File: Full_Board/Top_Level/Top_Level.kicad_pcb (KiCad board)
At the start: 2 copper layers, 187 parts, among them IC1 DRV8824QPWPRQ1, IC2 DRV8824QPWPRQ1, IC3 DRV8824QPWPRQ1, IC4 LM2576HVS-5.0_NOPB, IC5 CD74HC4051PWT, IC6 CD74HC4051PWT, IC7 DRV8210DRLR, J1 OQ0432500000G, J1-J3 Conn_01x10, J10 OQ0432500000G, J11 OQ0432500000G, J12 OQ0432500000G, J13 OQ0432500000G, J14 OQ0432500000G, J15 OQ0432500000G, J16 OQ0432500000G, J17 OQ0432500000G, J2 OQ0432500000G, J3 OQ0432500000G, J4 OQ0432500000G, J4-J2 Conn_01x10, J5 OQ0212500000G, J5-J7 Conn_01x10, J6 OQ0212500000G, J7 OQ0212500000G, J8 KLDHCX-8-0202-A, J8-J6 Conn_01x10, J9 OQ0212500000G, U1 LM2576SX-3.3-NOPB

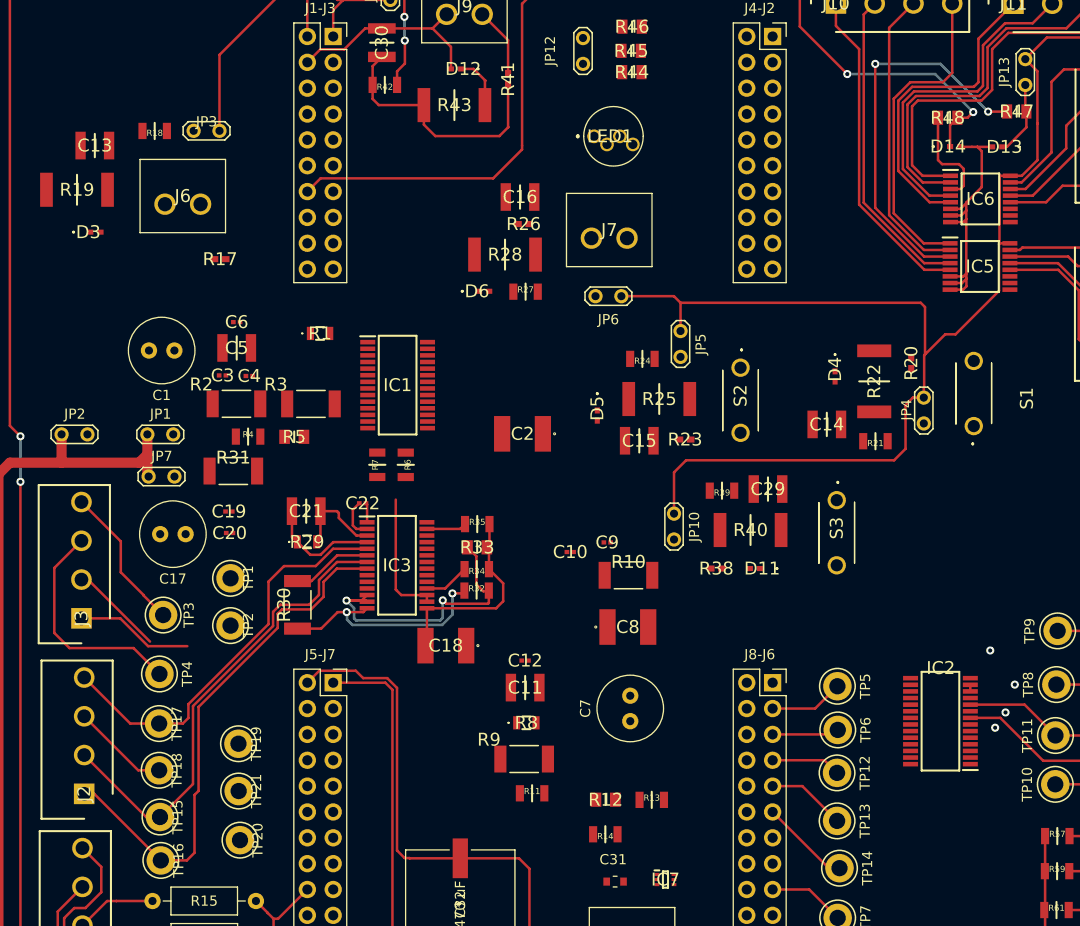
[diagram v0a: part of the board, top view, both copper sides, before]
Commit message: reed_switch_datasheet
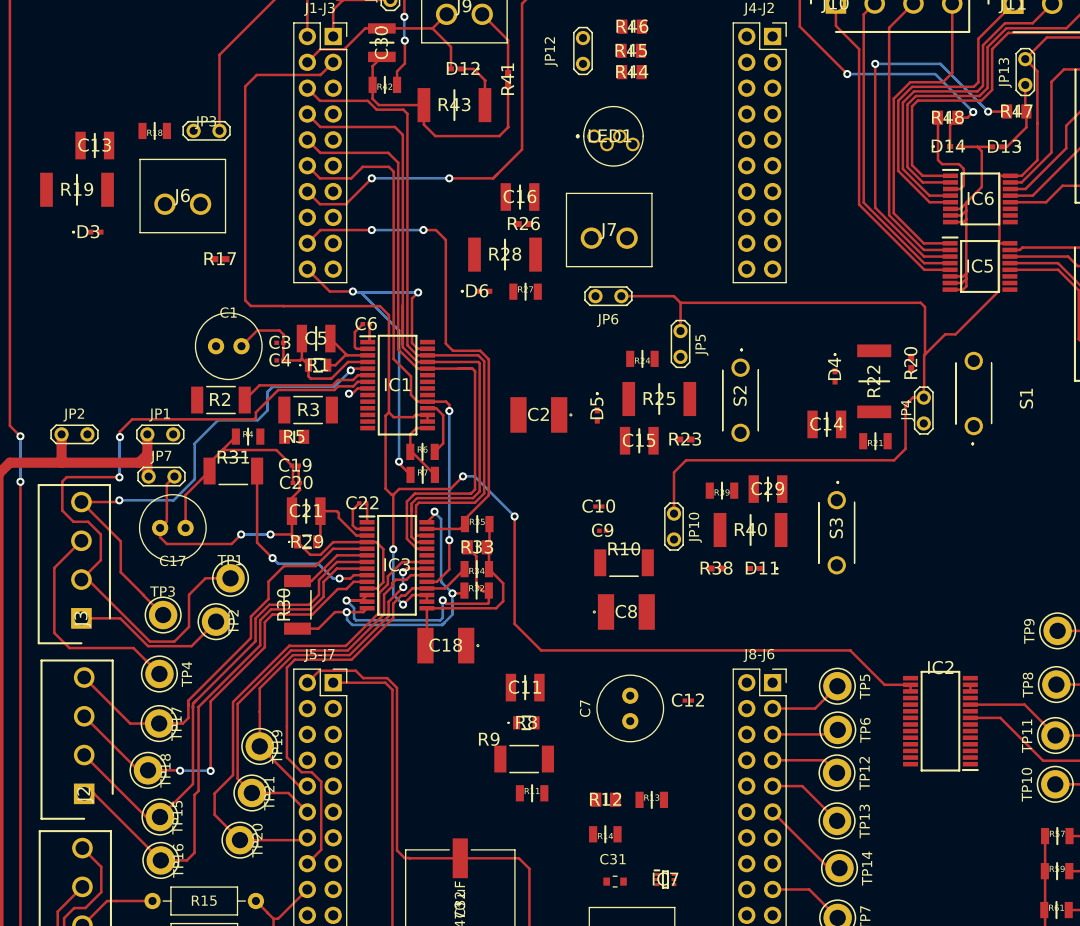
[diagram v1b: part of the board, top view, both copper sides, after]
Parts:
- moved C12 16.5 mm to (175.9, 86.9)
- moved C6 12.7 mm to (144.2, 49.9)
- moved C20 8.20 mm to (137.4, 65.5)
- moved C19 7.93 mm to (137.3, 63.8)
- moved C5 7.86 mm to (139.3, 51.3)
- moved C1 6.61 mm to (132.0, 52.1)
- moved C3 6.50 mm to (135.8, 51.7)
- moved R7 6.26 mm to (151.4, 65.5), turned to 180 degrees
- moved C10 5.28 mm to (167.1, 67.8)
- moved R6 4.55 mm to (151.4, 63.2), turned to 180 degrees
- moved C4 3.40 mm to (135.8, 53.5)
- moved R1 3.13 mm to (139.5, 53.9)
- moved C17 2.58 mm to (124.0, 69.9), turned to 0 degrees
- moved C2 2.45 mm to (161.2, 58.8)
- moved TP19 2.11 mm to (133.8, 91.4)
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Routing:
- net XYZ_RESET: track 12.8 -> 150.1 mm, vias 0 -> 4
- net XYZ_MS1: track 0.00 -> 68.2 mm
- net XYZ_MS2: track 0.00 -> 66.0 mm
- net XYZ_MS0: track 0.00 -> 62.7 mm
- net /StepperDriver2/2A: track 9.26 -> 71.5 mm, vias 0 -> 2
- net XYZ_DECAY: track 0.00 -> 55.5 mm, vias 0 -> 2
- net X_STEP: track 0.00 -> 48.4 mm
- net X_HOME: track 3.95 -> 50.7 mm, vias 0 -> 2
- net X_DIR: track 0.00 -> 40.7 mm
- net X_FAULT: track 4.49 -> 44.1 mm
- net Y_HOME: track 0.00 -> 38.8 mm, vias 0 -> 3
- net /StepperDriver2/1A: track 14.4 -> 51.1 mm, vias 0 -> 2
- net X_ENABLE: track 0.00 -> 35.0 mm, vias 0 -> 2
- net /StepperDriver1/1B: track 9.56 -> 43.2 mm, vias 0 -> 2
- net Net-(C17-Pad1): track 11.2 -> 43.2 mm, vias 0 -> 2
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
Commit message: Relayed out the power supply and stepper drivers
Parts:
- removed D1, D11, D12, D13, D14, D2, D3, D4, D5, D6: TPD1E10B06DPYR, TPD1E10B06DPYR:TPD1E10B06DPYR
- added J18: OQ0212500000G, OQ0212500000G:OQ0212500000G, F.Cu at (116.9, -114.6)
- added U10: UCLAMP3301H.TCT, UCLAMP3310H-TCT:UCLAMP3301H.TCT, F.Cu at (68.6, -124.2)
- added U11: UCLAMP3301H.TCT, UCLAMP3310H-TCT:UCLAMP3301H.TCT, F.Cu at (51.5, -115.7)
- added U12: UCLAMP3301H.TCT, UCLAMP3310H-TCT:UCLAMP3301H.TCT, F.Cu at (60.3, -83.8)
- added U2: UCLAMP3301H.TCT, UCLAMP3310H-TCT:UCLAMP3301H.TCT, F.Cu at (47.0, -79.7)
- added U3: UCLAMP3301H.TCT, UCLAMP3310H-TCT:UCLAMP3301H.TCT, F.Cu at (47.0, -70.9)
- added U4: UCLAMP3301H.TCT, UCLAMP3310H-TCT:UCLAMP3301H.TCT, F.Cu at (106.7, -59.2)
- added U5: UCLAMP3301H.TCT, UCLAMP3310H-TCT:UCLAMP3301H.TCT, F.Cu at (185.2, -124.2)
- added U6: UCLAMP3301H.TCT, UCLAMP3310H-TCT:UCLAMP3301H.TCT, F.Cu at (158.9, -99.6)
- added U7: UCLAMP3301H.TCT, UCLAMP3310H-TCT:UCLAMP3301H.TCT, F.Cu at (127.2, -97.9)
- added U8: UCLAMP3301H.TCT, UCLAMP3310H-TCT:UCLAMP3301H.TCT, F.Cu at (107.4, -40.4)
- added U9: UCLAMP3301H.TCT, UCLAMP3310H-TCT:UCLAMP3301H.TCT, F.Cu at (127.2, -79.1)
- J1: value OQ0432500000G -> USB_A; footprint OQ0432500000G:RHDR4W80P0X381_1X4_1540X700X920P -> USB1130-15-A:USB1130-15-A
- moved J17 316.8 mm to (35.0, -124.2), turned to 0 degrees
- moved J14 316.7 mm to (35.0, -107.1), turned to 0 degrees
- moved R55 312.5 mm to (41.4, -96.8), turned to 0 degrees
- moved R64 312.2 mm to (15.4, -94.2), turned to 0 degrees
- moved R53 312.0 mm to (45.9, -102.7), turned to 0 degrees
- moved R51 311.3 mm to (63.4, -116.5), turned to 0 degrees
- moved R49 307.9 mm to (41.4, -102.7), turned to 0 degrees
- moved R62 306.2 mm to (19.9, -94.2), turned to 0 degrees
- moved J15 300.9 mm to (17.9, -107.1), turned to 0 degrees
- moved R60 291.2 mm to (38.7, -93.9), turned to 0 degrees
- moved R58 290.7 mm to (58.5, -110.6), turned to 0 degrees
- moved R54 289.3 mm to (76.0, -128.4), turned to 0 degrees
- moved R56 284.4 mm to (45.9, -99.8), turned to 0 degrees
- moved R52 283.8 mm to (65.1, -119.6), turned to 0 degrees
- moved J16 282.7 mm to (35.0, -115.6), turned to 0 degrees
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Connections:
- C32 pad 1: +5.0V -> +5V
- J1 pad 1: /PiConnector1/Rx_Pi -> +3.3V
- J1 pad 2: /PiConnector1/Tx_Pi -> unconnected-(J1-Pad2)
- J1 pad 3: +3.3V -> unconnected-(J1-Pad3)
- J1-J3 pad 2: +5.0V -> /MSP432E401Y/+5V
- J5-J7 pad 2: +5.0V -> /MSP432E401Y/+5V
- JP9 pad 1: +5.0V -> +5V
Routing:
- net +3.3V: track 351.1 -> 0.00 mm, vias 2 -> 0
- net GND: track 257.4 -> 0.00 mm, vias 5 -> 0
- net +5.0V: track 251.3 -> 0.00 mm, vias 4 -> 0
- net +24V: track 235.2 -> 0.00 mm
- net XYZ_RESET: track 150.1 -> 0.00 mm, vias 4 -> 0
- net /StepperDriver2/2A: track 71.5 -> 0.00 mm, vias 2 -> 0
- net XYZ_MS1: track 68.2 -> 0.00 mm
- net XYZ_MS2: track 66.0 -> 0.00 mm
- net MUX_OUT: track 63.3 -> 0.00 mm, vias 2 -> 0
- net XYZ_MS0: track 62.7 -> 0.00 mm
- net Net-(C28-Pad1): track 58.2 -> 0.00 mm
- net XYZ_DECAY: track 55.5 -> 0.00 mm, vias 2 -> 0
- net /StepperDriver1/2B: track 52.8 -> 0.00 mm
- net /StepperDriver2/1A: track 51.1 -> 0.00 mm, vias 2 -> 0
- net X_HOME: track 50.7 -> 0.00 mm, vias 2 -> 0
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- removed copper zone on B.Cu, net GND
- removed copper zone on F.Cu, net GND

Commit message: More layout work
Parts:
- moved J2 245.6 mm to (175.5, 113.7), turned to 90 degrees
- moved J18 212.1 mm to (50.9, 86.9)
- moved J5 212.1 mm to (39.4, 86.9)
- moved J4 211.5 mm to (125.7, 83.8), turned to 90 degrees
- moved J3 170.3 mm to (138.0, 42.8), turned to -90 degrees
- moved TP3 54.6 mm to (131.6, 55.4)
- moved TP2 53.0 mm to (131.6, 40.9)
- moved TP4 50.5 mm to (131.6, 50.5)
- moved TP1 49.9 mm to (131.6, 45.7)
- moved TP9 41.2 mm to (118.1, 85.6)
- moved TP11 30.6 mm to (118.1, 76.2)
- moved TP15 28.4 mm to (166.9, 110.7)
- moved JP2 27.5 mm to (99.5, 66.6), turned to -90 degrees
- moved JP1 27.1 mm to (102.4, 37.1), turned to -90 degrees
- moved JP7 26.2 mm to (102.2, 98.9), turned to -90 degrees
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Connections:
- J1 pad 1: +3.3V -> /PiConnector1/5V
- U12 pad 2: +3.3V -> /PiConnector1/5V

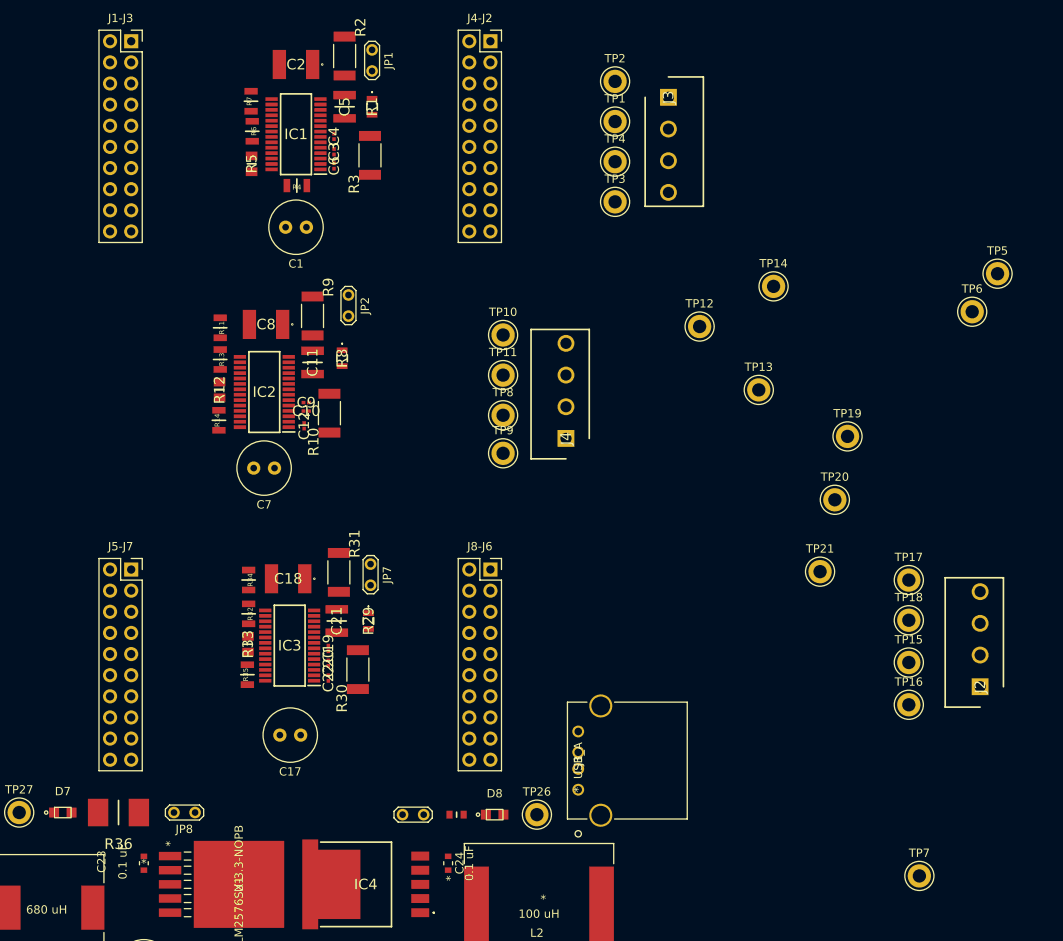
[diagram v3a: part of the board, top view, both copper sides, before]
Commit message: Layed out stepper connectors and test points
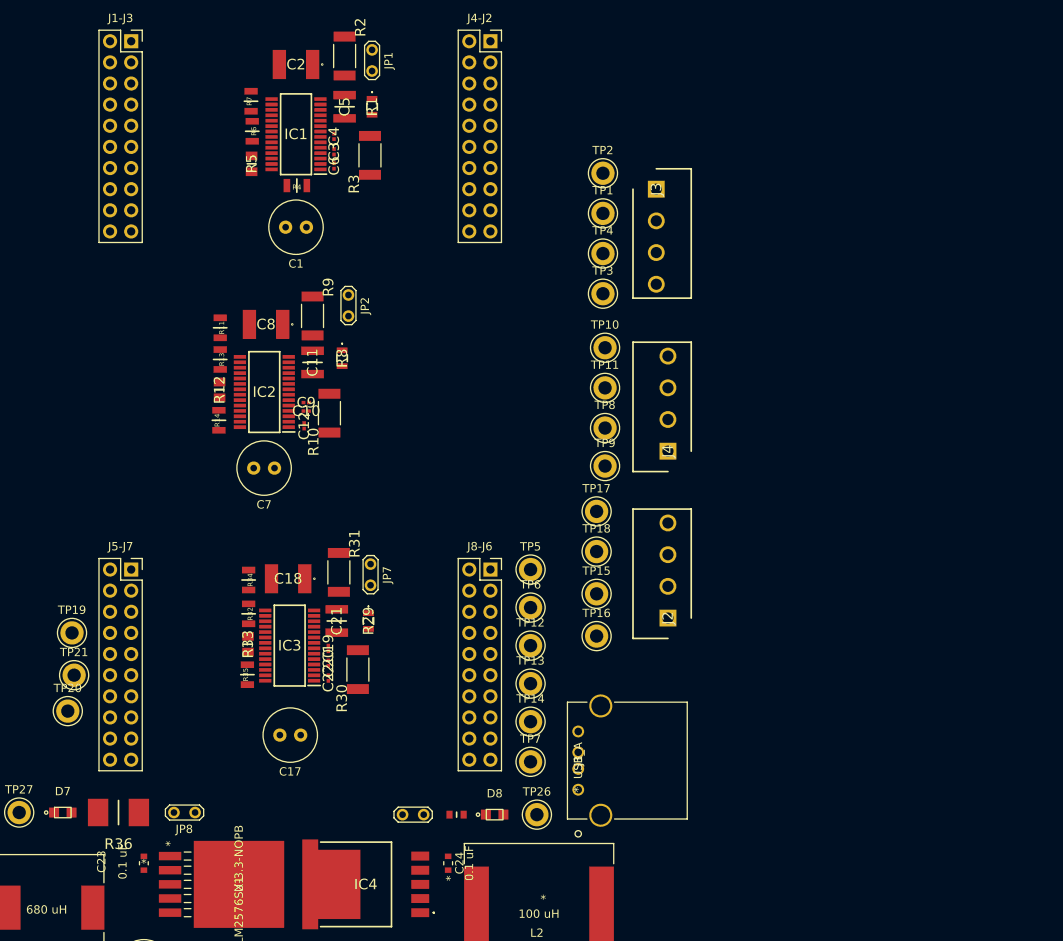
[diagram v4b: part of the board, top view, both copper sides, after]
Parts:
- moved TP19 96.2 mm to (66.3, 107.2)
- moved TP20 95.6 mm to (65.8, 116.6)
- moved TP21 90.5 mm to (66.5, 112.3)
- moved TP5 66.4 mm to (121.4, 99.6)
- moved TP6 63.9 mm to (121.4, 104.1)
- moved TP14 59.9 mm to (121.4, 117.9)
- moved TP7 48.7 mm to (121.4, 122.7)
- moved TP13 44.7 mm to (121.4, 113.3)
- moved TP12 43.4 mm to (121.4, 108.7)
- moved J2 38.4 mm to (137.9, 105.4)
- moved TP15 38.4 mm to (129.4, 102.5)
- moved TP16 38.4 mm to (129.4, 107.6)
- moved TP17 38.4 mm to (129.4, 92.6)
- moved TP18 38.4 mm to (129.4, 97.4)
- moved J4 12.4 mm to (137.9, 85.3)
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
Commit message: Redo pinout, finish pcb layout (no traces)
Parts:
- removed the C29 at (110.1, -34.5)
- removed the JP10 at (103.2, -34.8)
- removed the R38 at (103.1, -37.6)
- removed the R39 at (93.3, -33.0)
- removed the R40 at (97.0, -36.2)
- removed the TP1 at (130.1, 56.8)
- removed the TP10 at (130.4, 72.9)
- removed the TP11 at (130.4, 77.7)
- removed the TP15 at (129.4, 102.5)
- removed TP16, TP17, TP18: TestPoint, TestPoint:TestPoint_Keystone_5010-5014_Multipurpose
- removed the TP2 at (130.1, 51.9)
- removed the TP3 at (130.1, 66.4)
- removed the TP4 at (130.1, 61.6)
- removed the TP8 at (130.4, 82.6)
- removed the TP9 at (130.4, 87.1)
- removed the U12 at (60.3, -83.8)
- removed the U6 at (158.9, -99.6)
- added C17: 8200pF, C1210C822K2RACAUTO:CAPC3225X88N, F.Cu at (72.2, 55.6)
- added C18: 8200pF, C1210C822K2RACAUTO:CAPC3225X88N, F.Cu at (57.5, 137.9)
- added C31: 8200pF, C1210C822K2RACAUTO:CAPC3225X88N, F.Cu at (82.3, 41.4)
- added C35: 8200pF, C1210C822K2RACAUTO:CAPC3225X88N, F.Cu at (71.0, 48.0)
- added C36: 8200pF, C1210C822K2RACAUTO:CAPC3225X88N, F.Cu at (71.0, 91.7)
- added C37: 8200pF, C1210C822K2RACAUTO:CAPC3225X88N, F.Cu at (71.4, 117.3)
- added C38: 8200pF, C1210C822K2RACAUTO:CAPC3225X88N, F.Cu at (71.2, 106.7)
- added J21: OQ0212500000G, OQ0212500000G:OQ0212500000G, F.Cu at (59.7, 49.6)
- added J22: OQ0212500000G, OQ0212500000G:OQ0212500000G, F.Cu at (59.7, 94.5)
- added J23: OQ0212500000G, OQ0212500000G:OQ0212500000G, F.Cu at (59.7, 116.9)
- added J24: OQ0212500000G, OQ0212500000G:OQ0212500000G, F.Cu at (59.7, 105.7)
- added J9: OQ0212500000G, OQ0212500000G:OQ0212500000G, F.Cu at (59.5, 128.0)
- added JP12: 3.3V Jumper, TestPoint:TestPoint_2Pads_Pitch2.54mm_Drill0.8mm, F.Cu at (68.2, 27.4)
- added JP17: 3.3V Jumper, TestPoint:TestPoint_2Pads_Pitch2.54mm_Drill0.8mm, F.Cu at (67.7, 54.1)
- added JP18: 3.3V Jumper, TestPoint:TestPoint_2Pads_Pitch2.54mm_Drill0.8mm, F.Cu at (67.3, 98.5)
- added JP19: 3.3V Jumper, TestPoint:TestPoint_2Pads_Pitch2.54mm_Drill0.8mm, F.Cu at (67.1, 120.4)
- added JP20: 3.3V Jumper, TestPoint:TestPoint_2Pads_Pitch2.54mm_Drill0.8mm, F.Cu at (67.1, 107.9)
- added JP7: 3.3V Jumper, TestPoint:TestPoint_2Pads_Pitch2.54mm_Drill0.8mm, F.Cu at (67.1, 31.5)
- added JP8: 3.3V Jumper, TestPoint:TestPoint_2Pads_Pitch2.54mm_Drill0.8mm, F.Cu at (66.9, 131.1)
- added R29: 562, CR0402-FX-5620GLF:RESC1005X40N, F.Cu at (76.3, 52.1)
- added R30: 10k, RMCF1206FT10K0:RMCF1206FT10K0, F.Cu at (84.4, 54.1)
- added R31: 100k, RCV2512100KFKEGAT:RESC6332X70N, F.Cu at (78.1, 55.6)
- added R32: 562, CR0402-FX-5620GLF:RESC1005X40N, F.Cu at (61.6, 141.2)
- added R33: 10k, RMCF1206FT10K0:RMCF1206FT10K0, F.Cu at (64.9, 140.2)
- added R34: 100k, RCV2512100KFKEGAT:RESC6332X70N, F.Cu at (64.4, 137.4)
- added R44: 562, CR0402-FX-5620GLF:RESC1005X40N, F.Cu at (75.0, 41.9)
- added R45: 10k, RMCF1206FT10K0:RMCF1206FT10K0, F.Cu at (77.0, 43.2)
- added R46: 100k, RCV2512100KFKEGAT:RESC6332X70N, F.Cu at (80.6, 46.0)
- added R71: 562, CR0402-FX-5620GLF:RESC1005X40N, F.Cu at (67.1, 47.2)
- added R72: 10k, RMCF1206FT10K0:RMCF1206FT10K0, F.Cu at (69.5, 39.4)
- added R73: 100k, RCV2512100KFKEGAT:RESC6332X70N, F.Cu at (69.2, 43.9)
- added R74: 562, CR0402-FX-5620GLF:RESC1005X40N, F.Cu at (70.6, 94.7)
- added R75: 10k, RMCF1206FT10K0:RMCF1206FT10K0, F.Cu at (75.9, 90.2)
- added R76: 100k, RCV2512100KFKEGAT:RESC6332X70N, F.Cu at (72.9, 98.0)
- added R77: 562, CR0402-FX-5620GLF:RESC1005X40N, F.Cu at (70.6, 120.4)
- added R78: 10k, RMCF1206FT10K0:RMCF1206FT10K0, F.Cu at (74.5, 121.4)
- added R79: 100k, RCV2512100KFKEGAT:RESC6332X70N, F.Cu at (73.2, 113.3)
- added R80: 562, CR0402-FX-5620GLF:RESC1005X40N, F.Cu at (70.6, 109.2)
- added R81: 10k, RMCF1206FT10K0:RMCF1206FT10K0, F.Cu at (73.9, 105.7)
- added R82: 100k, RCV2512100KFKEGAT:RESC6332X70N, F.Cu at (72.9, 102.9)
- added U11: UCLAMP3301H.TCT, UCLAMP3310H-TCT:UCLAMP3301H.TCT, F.Cu at (75.0, 46.0)
- added U15: UCLAMP3301H.TCT, UCLAMP3310H-TCT:UCLAMP3301H.TCT, F.Cu at (71.5, 37.8)
- added U16: UCLAMP3301H.TCT, UCLAMP3310H-TCT:UCLAMP3301H.TCT, F.Cu at (74.9, 94.7)
- added U17: UCLAMP3301H.TCT, UCLAMP3310H-TCT:UCLAMP3301H.TCT, F.Cu at (72.1, 116.8)
- added U18: UCLAMP3301H.TCT, UCLAMP3310H-TCT:UCLAMP3301H.TCT, F.Cu at (75.2, 109.2)
- added U4: UCLAMP3301H.TCT, UCLAMP3310H-TCT:UCLAMP3301H.TCT, F.Cu at (74.5, 37.1)
- added U7: JS102011SCQN, JS102011SCQN:JS102011SCQN, F.Cu at (60.0, 31.8)
- added U9: UCLAMP3301H.TCT, UCLAMP3310H-TCT:UCLAMP3301H.TCT, F.Cu at (56.7, 141.0)
- moved R70 248.4 mm to (128.1, 127.2), turned to 90 degrees
- moved R68 247.6 mm to (130.6, 127.2), turned to 90 degrees
- moved U14 246.7 mm to (131.2, 117.9), turned to 180 degrees
- moved U13 246.2 mm to (126.3, 115.1), turned to -90 degrees
- moved R53 241.4 mm to (129.6, 115.3), turned to 180 degrees
- moved JP16 240.1 mm to (126.8, 111.7), turned to 90 degrees
- moved R61 237.2 mm to (130.6, 122.9), turned to 90 degrees
- moved R60 237.1 mm to (121.3, 104.4)
- moved R65 236.8 mm to (121.3, 112.0)
- moved R63 236.4 mm to (121.3, 114.5)
- moved R64 236.1 mm to (121.3, 117.1)
- moved R66 234.5 mm to (128.1, 122.9), turned to 90 degrees
- moved R67 234.3 mm to (125.8, 117.1)
- moved R58 233.3 mm to (121.3, 106.9)
- moved R57 233.2 mm to (121.3, 109.4)
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- renumbered C17 to C19, C18 to C20, C19 to C21, C20 to C22, C21 to C23, C22 to C24, C23 to C25, C24 to C26, C25 to C27, C26 to C28, C27 to C29, C28 to C30, C30 to C32, C31 to C33, C32 to C34, D7 to D1, D8 to D2, D9 to D3, D10 to D4, J18 to J1, J1-J3 to J1-J1, J8 to J10, J9 to J11, J10 to J12, J11 to J13, J12 to J15, J13 to J16, J14 to J17, J15 to J18, J16 to J19, J5 to J2, J17 to J20, J2 to J3, J3 to J4, J4-J2 to J4-J1, J4 to J5, J5-J7 to J5-J1, J1 to J6, J6 to J7, J7 to J8, J8-J6 to J8-J1, JP8 to JP10, JP9 to JP11, JP11 to JP13, JP12 to JP14, JP13 to JP15, JP14 to JP16, JP7 to JP9, R29 to R35, R30 to R36, R31 to R37, R32 to R38, R33 to R39, R34 to R40, R35 to R41, R36 to R42, R37 to R43, R41 to R47, R42 to R48, R43 to R49, R44 to R50, R45 to R51, R46 to R52, R47 to R53, R48 to R54, R49 to R55, R50 to R56, R51 to R57, R52 to R58, R53 to R59, R54 to R60, R55 to R61, R56 to R62, R57 to R63, R58 to R64, R59 to R65, R60 to R66, R61 to R67, R62 to R68, R63 to R69, R64 to R70, TP5 to TP1, TP25 to TP10, TP23 to TP11, TP22 to TP12, TP24 to TP13, TP26 to TP14, TP27 to TP15, TP6 to TP2, TP7 to TP3, TP12 to TP4, TP13 to TP5, TP14 to TP6, TP19 to TP7, TP20 to TP8, TP21 to TP9, U2 to U1, U1 to U10, U9 to U12, U10 to U13, U11 to U14, U3 to U2, U4 to U3, U7 to U6
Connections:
- IC1 pad 24: XYZ_MS0 -> XY_MS0
- IC1 pad 25: XYZ_MS1 -> XY_MS1
- IC1 pad 26: XYZ_MS2 -> XY_MS2
- IC2 pad 24: XYZ_MS0 -> Z_MS0
- IC2 pad 25: XYZ_MS1 -> Z_MS1
- IC2 pad 26: XYZ_MS2 -> Z_MS2
- IC3 pad 24: XYZ_MS0 -> XY_MS0
- IC3 pad 25: XYZ_MS1 -> XY_MS1
- IC3 pad 26: XYZ_MS2 -> XY_MS2
- J1-J1 pad 10: XYZ_MS0 -> Z_STEP
- J1-J1 pad 11: /MSP432E401Y/PE_5 -> Z_MS1
- J1-J1 pad 13: MUX_S0 -> Z_MS0
- J1-J1 pad 14: MUX_OUT -> XYZ_RESET
- J1-J1 pad 15: /MSP432E401Y/PC_7 -> LED_R
- J1-J1 pad 16: /MSP432E401Y/PA_6 -> XY_MS2
- J1-J1 pad 17: /MSP432E401Y/PB_2 -> LED_B
- J1-J1 pad 18: X_HOME -> XY_MS1
- J1-J1 pad 19: /MSP432E401Y/PB_3 -> LED_G
- J1-J1 pad 20: Y_HOME -> XY_MS0
- J1-J1 pad 3: XYZ_RESET -> Y_ENABLE
- J1-J1 pad 5: /MSP432E401Y/PC_4 -> Y_DIR
- J1-J1 pad 6: XYZ_MS2 -> Z_ENABLE
- J1-J1 pad 7: /MSP432E401Y/PC_5 -> Y_STEP
- J1-J1 pad 8: XYZ_MS1 -> Z_DIR
- J1-J1 pad 9: /MSP432E401Y/PC_6 -> Z_MS2
- J4-J1 pad 1: BLUE_WAIT -> X_FAULT
- J4-J1 pad 11: RESET_OUT -> Z_FAULT
- J4-J1 pad 12: DEMUX_S1 -> /MSP432E401Y/PD_1
- J4-J1 pad 13: HOME_OUT -> MUX_OUT
- J4-J1 pad 14: DEMUX_S0 -> /MSP432E401Y/PD_0
- J4-J1 pad 15: LS_Z_OUT -> CAPTURE_OUT
- J4-J1 pad 17: LS_Y_OUT -> /MSP432E401Y/PL_2
- J4-J1 pad 19: LS_X_OUT -> /MSP432E401Y/PL_3
- J4-J1 pad 3: GREEN_TAKE_TURN -> X_HOME
- J4-J1 pad 4: Z_FAULT -> /MSP432E401Y/PM_3
- J4-J1 pad 5: RED_ERROR -> Y_HOME
- J4-J1 pad 7: /MSP432E401Y/PG_0 -> Y_FAULT
- J4-J1 pad 9: START_OUT -> Z_HOME
- J5-J1 pad 10: X_ENABLE -> LS_Z_OUT
- J5-J1 pad 11: MUX_S2 -> DEMUX_S1
- J5-J1 pad 12: X_DIR -> LS_Y_OUT
- J5-J1 pad 13: /MSP432E401Y/PQ_0 -> DEMUX_S0
- J5-J1 pad 14: X_STEP -> LS_X_OUT
- J5-J1 pad 15: /MSP432E401Y/PP_4 -> MUX_S2
- J5-J1 pad 16: X_FAULT -> HOME_OUT
- J5-J1 pad 17: /MSP432E401Y/PN_5 -> MUX_S1
- J5-J1 pad 19: /MSP432E401Y/PN_4 -> MUX_S0
- J5-J1 pad 3: DEMUX_S2 -> X_ENABLE
- J5-J1 pad 5: /MSP432E401Y/PP_0 -> X_DIR
- J5-J1 pad 6: /MSP432E401Y/PB_4 -> MAG_IN1
- J5-J1 pad 7: /MSP432E401Y/PP_1 -> X_STEP
- J5-J1 pad 8: /MSP432E401Y/PB_5 -> MAG_IN2
- J5-J1 pad 9: MUX_S1 -> DEMUX_S2
- J6 pad 6: (no net) -> unconnected-(J6-Pad6)
- J8-J1 pad 11: Z_DIR -> FP_3_OUT
- J8-J1 pad 13: MAG_IN1 -> /MSP432E401Y/PH_0
- J8-J1 pad 15: MAG_IN2 -> /MSP432E401Y/PH_1
- J8-J1 pad 17: Y_DIR -> COLOR_OUT
- J8-J1 pad 19: Y_FAULT -> NEXT_TURN_OUT
- J8-J1 pad 3: Y_ENABLE -> RESET_OUT
- J8-J1 pad 4: Z_HOME -> /MSP432E401Y/PM_7
- J8-J1 pad 5: Y_STEP -> START_OUT
- J8-J1 pad 7: Z_ENABLE -> FP_1_OUT
- J8-J1 pad 9: Z_STEP -> FP_2_OUT
- R50 pad 1: BLUE_WAIT -> LED_B
- R51 pad 1: GREEN_TAKE_TURN -> LED_G
- R52 pad 1: RED_ERROR -> LED_R
- U5 pad 2: RESET_OUT -> HOME_OUT
- U8 pad 2: START_OUT -> COLOR_OUT
